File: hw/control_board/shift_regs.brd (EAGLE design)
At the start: 164.8 x 50.2 mm, 137 parts, among them IC1 74HC595D, IC13 STM32F10XCXT6, IC2 74HC595D, IC3 74HC595D, IC4 74HC595D, IC5 74HC595D, IC6 74HC595D, IC7 74HC595D, IC8 74HC595D, IC9 ESP8266, Q1 4MHz, Q2 32768KHz, T1 BC847, T10 BC847, T11 BC847, T12 BC847, T13 BC847, T14 BC847, T15 BC847, T16 BC847, T2 BC847, T3 BC847, T4 BC847, T5 BC847, T6 BC847, T7 BC847, T8 BC847, T9 BC847

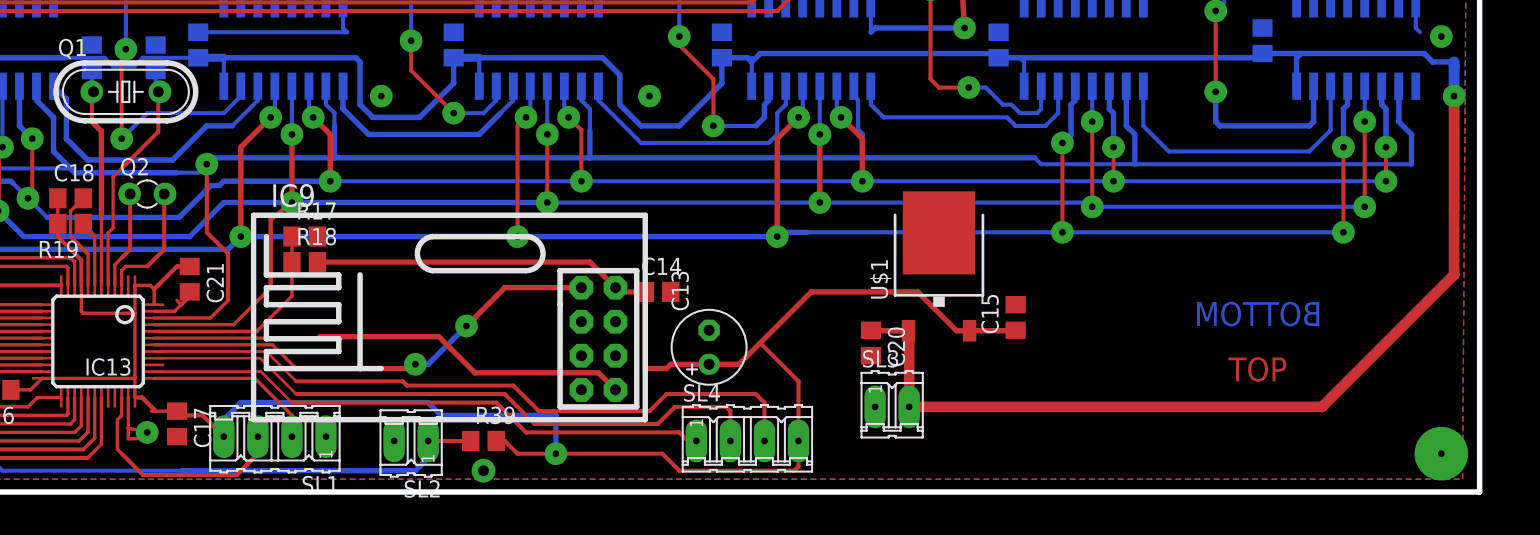
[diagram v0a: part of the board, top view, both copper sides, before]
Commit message: added control buttons to the control PCB
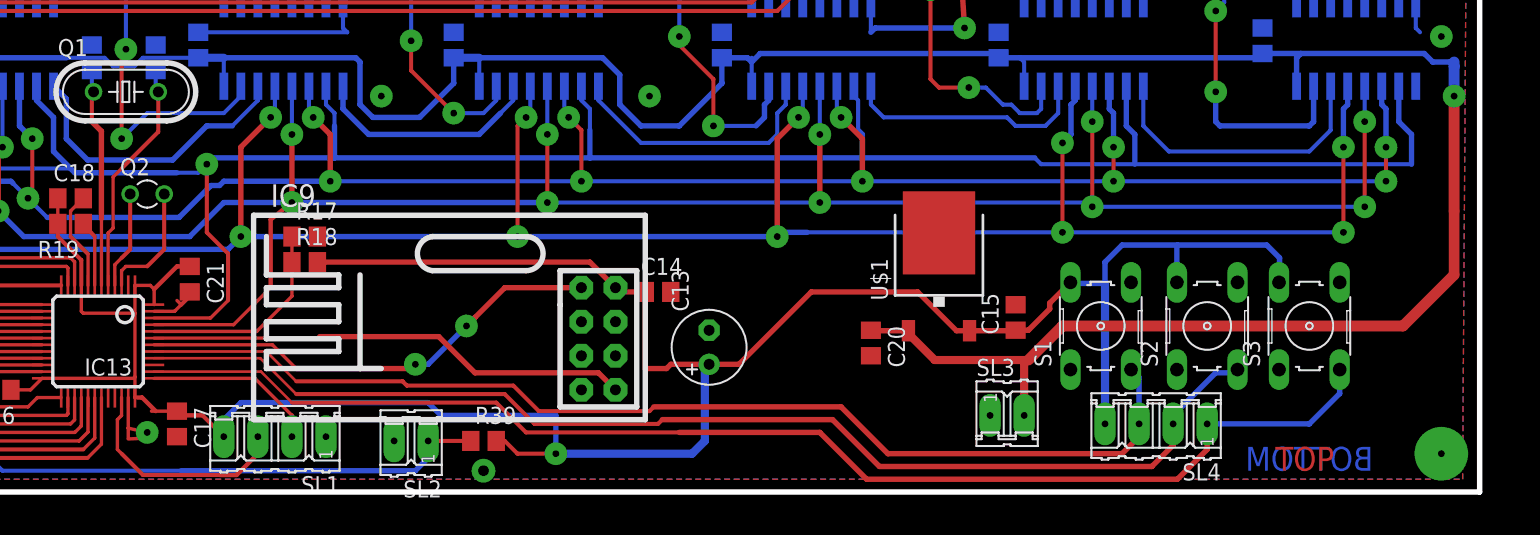
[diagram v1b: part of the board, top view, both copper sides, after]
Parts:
- added S1, S2, S3: (no value), switch-omron:B3F-10XX
- moved SL4 30.5 mm to (140.7, 5.40), turned to 180 degrees
- moved SL3 8.60 mm to (129.5, 6.03)
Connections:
- net +3V3: now also S1.2, S2.2, S3.2
- net BUTT_ENTER: now also S2.3
- net BUTT_LEFT: now also S3.3
- net BUTT_RIGHT: now also S1.3
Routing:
- net BUTT_LEFT: track 42.6 -> 97.3 mm
- net BUTT_ENTER: track 47.9 -> 88.7 mm
- net BUTT_RIGHT: track 51.0 -> 82.7 mm
- net +3V3: track 172.2 -> 200.0 mm
- net +9V: track 267.5 -> 266.6 mm
